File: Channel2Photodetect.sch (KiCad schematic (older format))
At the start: 5 parts

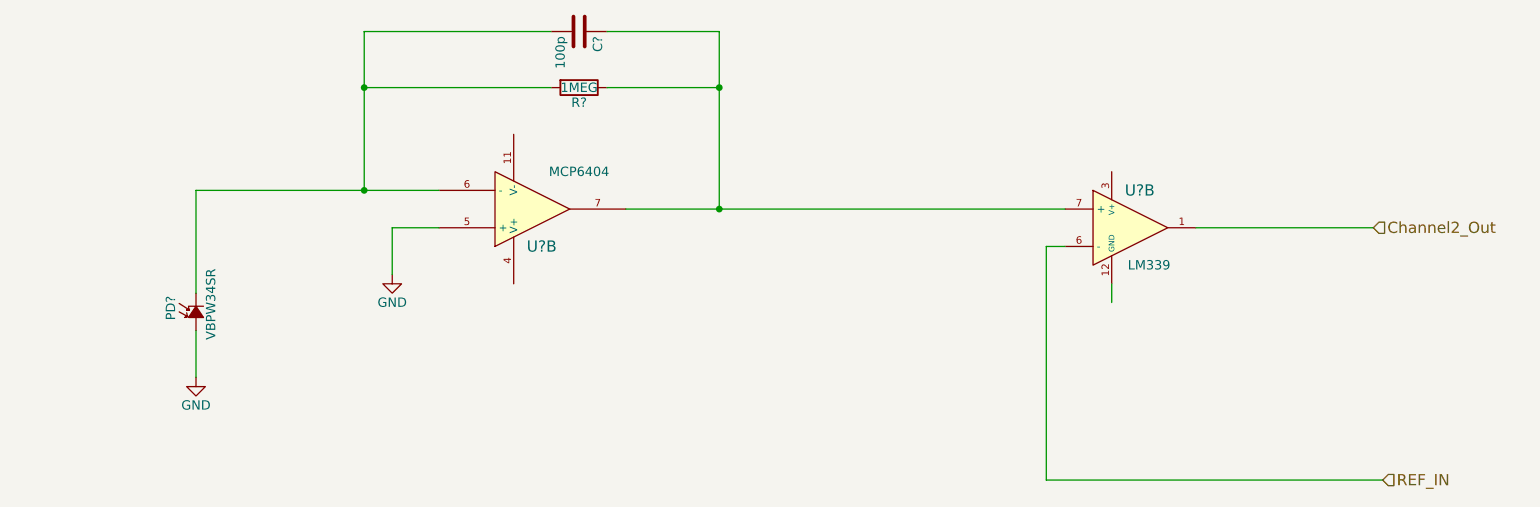
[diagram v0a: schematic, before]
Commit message: Added power regulator, VGND and test points
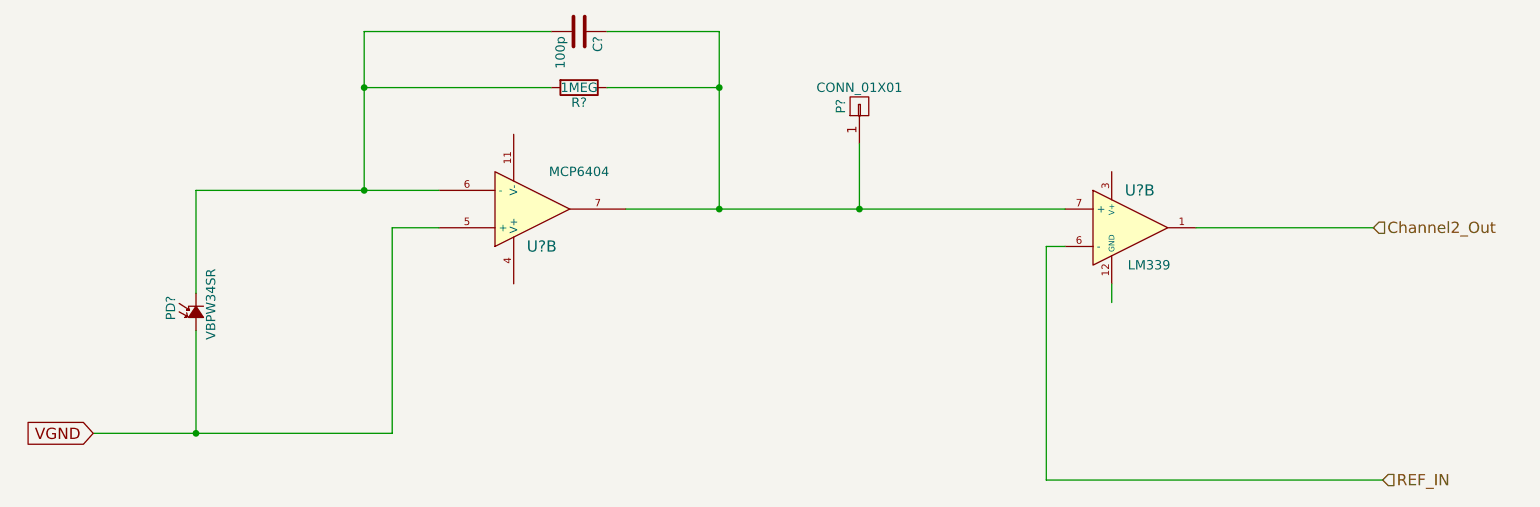
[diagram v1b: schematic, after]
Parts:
- added P?: CONN_01X01, symbol CONN_01X01
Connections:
- net labels added: VGND
- net labels removed: GND
- wire segments 17 -> 19
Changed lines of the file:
@@
 LIBS:memory
 LIBS:xilinx
-LIBS:special
 LIBS:microcontrollers
 LIBS:dsp
@@
 	4850 2200 5450 2200
 Connection ~ 5450 2500
-$Comp
-L GND #PWR?
-U 1 1 5552E303
-P 3700 3500
-F 0 "#PWR?" H 3700 3250 50  0001 C CNN
-F 1 "GND" H 3700 3350 50  0000 C CNN
-F 2 "" H 3700 3500 60  0000 C CNN
-F 3 "" H 3700 3500 60  0000 C CNN
-	1    3700 3500
-	1    0    0    -1
-$EndComp
 Wire Wire Line
 	3950 3250 3700 3250
 Wire Wire Line
-	3700 3250 3700 3500
-$Comp
-L GND #PWR?
-U 1 1 5552E31E
-P 2650 4050
-F 0 "#PWR?" H 2650 3800 50  0001 C CNN
-F 1 "GND" H 2650 3900 50  0000 C CNN
-F 2 "" H 2650 4050 60  0000 C CNN
-F 3 "" H 2650 4050 60  0000 C CNN
-	1    2650 4050
-	1    0    0    -1
-$EndComp
+	3700 3250 3700 4350
 Wire Wire Line
-	2650 3800 2650 4050
+	2650 3800 2650 4350
 $Comp
 L LM339 U?
@@
 Wire Wire Line
 	7200 4600 7200 3350
+Wire Wire Line
+	3700 4350 2100 4350
+Text GLabel 2100 4350 0    60   Input ~ 0
+VGND
+Connection ~ 2650 4350
+$Comp
+L CONN_01X01 P?
+U 1 1 55563262
+P 6200 2600
+F 0 "P?" H 6200 2700 50  0000 C CNN
+F 1 "CONN_01X01" V 6300 2600 50  0000 C CNN
+F 2 "" H 6200 2600 60  0000 C CNN
+F 3 "" H 6200 2600 60  0000 C CNN
+	1    6200 2600
+	0    -1   -1   0
+$EndComp
+Wire Wire Line
+	6200 2800 6200 3150
+Connection ~ 6200 3150
 $EndSCHEMATC

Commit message: Added libraries and imported components into the layout
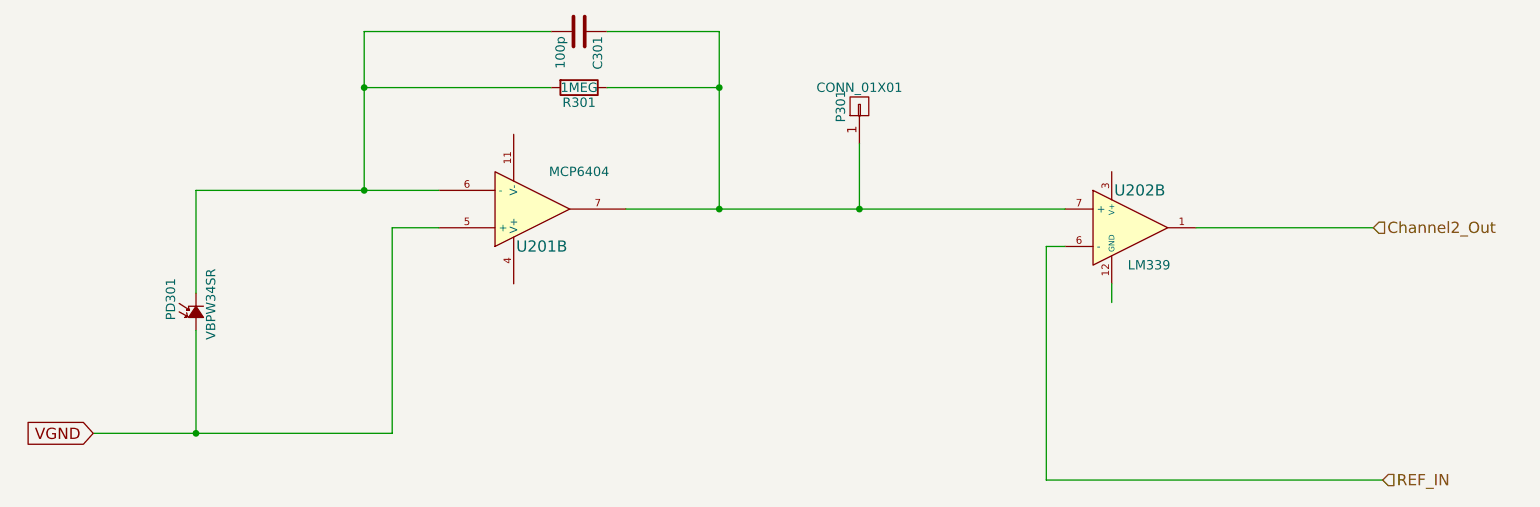
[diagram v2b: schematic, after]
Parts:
- gave numbers to parts that had none: 6
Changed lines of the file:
@@
 $EndDescr
 $Comp
-L R R?
+L R R301
 U 1 1 5552E2CE
 P 4700 2500
-F 0 "R?" V 4780 2500 50  0000 C CNN
+F 0 "R301" V 4780 2500 50  0000 C CNN
 F 1 "1MEG" V 4700 2500 50  0000 C CNN
 F 2 "" V 4630 2500 30  0000 C CNN
@@
 $EndComp
 $Comp
-L C C?
+L C C301
 U 1 1 5552E2D5
 P 4700 2200
-F 0 "C?" H 4725 2300 50  0000 L CNN
+F 0 "C301" H 4725 2300 50  0000 L CNN
 F 1 "100p" H 4725 2100 50  0000 L CNN
 F 2 "" H 4738 2050 30  0000 C CNN
@@
 $EndComp
 $Comp
-L MCP6404-E/SL U?
+L MCP6404-E/SL U201
 U 2 1 5552E2DE
 P 4450 3150
-F 0 "U?" H 4500 3350 60  0000 C CNN
+F 0 "U201" H 4500 3350 60  0000 C CNN
 F 1 "MCP6404" H 4700 2950 50  0000 C CNN
 F 2 "" H 4450 3150 60  0000 C CNN
@@
 $EndComp
 $Comp
-L Photodiode PD?
+L Photodiode PD301
 U 1 1 5552E2E7
 P 2650 3700
-F 0 "PD?" H 2605 3835 50  0000 L CNN
+F 0 "PD301" H 2605 3835 50  0000 L CNN
 F 1 "VBPW34SR" H 2500 3620 50  0000 L CNN
 F 2 "" V 2650 3700 60  0000 C CNN
@@
 	2650 3800 2650 4350
 $Comp
-L LM339 U?
+L LM339 U202
 U 2 1 5552E327
 P 7650 3250
-F 0 "U?" H 7700 3450 60  0000 C CNN
+F 0 "U202" H 7700 3450 60  0000 C CNN
 F 1 "LM339" H 7750 3050 50  0000 C CNN
 F 2 "" H 7650 3250 60  0000 C CNN
@@
 Connection ~ 2650 4350
 $Comp
-L CONN_01X01 P?
+L CONN_01X01 P301
 U 1 1 55563262
 P 6200 2600
-F 0 "P?" H 6200 2700 50  0000 C CNN
+F 0 "P301" H 6200 2700 50  0000 C CNN
 F 1 "CONN_01X01" V 6300 2600 50  0000 C CNN
 F 2 "" H 6200 2600 60  0000 C CNN

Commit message: Added photodiode component to new local footprint library
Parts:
- C301: footprint (none) -> Capacitors_SMD:C_0805_HandSoldering
- P301: footprint (none) -> Pin_Headers:Pin_Header_Straight_1x01
- PD301: footprint (none) -> DasBlinkinput:VPW34SR
- R301: footprint (none) -> Resistors_SMD:R_1206_HandSoldering
- U201, U202: footprint (none) -> Housings_SOIC:SOIC-14_3.9x8.7mm_Pitch1.27mm
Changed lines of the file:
@@
 F 0 "R301" V 4780 2500 50  0000 C CNN
 F 1 "1MEG" V 4700 2500 50  0000 C CNN
-F 2 "" V 4630 2500 30  0000 C CNN
+F 2 "Resistors_SMD:R_1206_HandSoldering" V 4630 2500 30  0001 C CNN
 F 3 "" H 4700 2500 30  0000 C CNN
 F 4 "RC1206FR-071ML" V 4700 2500 60  0001 C CNN "MPN"
@@
 F 0 "C301" H 4725 2300 50  0000 L CNN
 F 1 "100p" H 4725 2100 50  0000 L CNN
-F 2 "" H 4738 2050 30  0000 C CNN
+F 2 "Capacitors_SMD:C_0805_HandSoldering" H 4738 2050 30  0001 C CNN
 F 3 "" H 4700 2200 60  0000 C CNN
 	1    4700 2200
@@
 F 0 "U201" H 4500 3350 60  0000 C CNN
 F 1 "MCP6404" H 4700 2950 50  0000 C CNN
-F 2 "" H 4450 3150 60  0000 C CNN
+F 2 "Housings_SOIC:SOIC-14_3.9x8.7mm_Pitch1.27mm" H 4450 3150 60  0001 C CNN
 F 3 "" H 4450 3150 60  0000 C CNN
 F 4 "MCP6404-E/SL" H 4450 3150 60  0001 C CNN "MPN"
@@
 F 0 "PD301" H 2605 3835 50  0000 L CNN
 F 1 "VBPW34SR" H 2500 3620 50  0000 L CNN
-F 2 "" V 2650 3700 60  0000 C CNN
+F 2 "DasBlinkinput:VPW34SR" V 2650 3700 60  0001 C CNN
 F 3 "" V 2650 3700 60  0000 C CNN
 F 4 "VBPW34SR" H 2650 3700 60  0001 C CNN "MPN"
@@
 F 0 "U202" H 7700 3450 60  0000 C CNN
 F 1 "LM339" H 7750 3050 50  0000 C CNN
-F 2 "" H 7650 3250 60  0000 C CNN
+F 2 "Housings_SOIC:SOIC-14_3.9x8.7mm_Pitch1.27mm" H 7650 3250 60  0001 C CNN
 F 3 "" H 7650 3250 60  0000 C CNN
 F 4 "LM339DE4" H 7650 3250 60  0001 C CNN "MPN"
@@
 F 0 "P301" H 6200 2700 50  0000 C CNN
 F 1 "CONN_01X01" V 6300 2600 50  0000 C CNN
-F 2 "" H 6200 2600 60  0000 C CNN
+F 2 "Pin_Headers:Pin_Header_Straight_1x01" H 6200 2600 60  0001 C CNN
 F 3 "" H 6200 2600 60  0000 C CNN
 	1    6200 2600

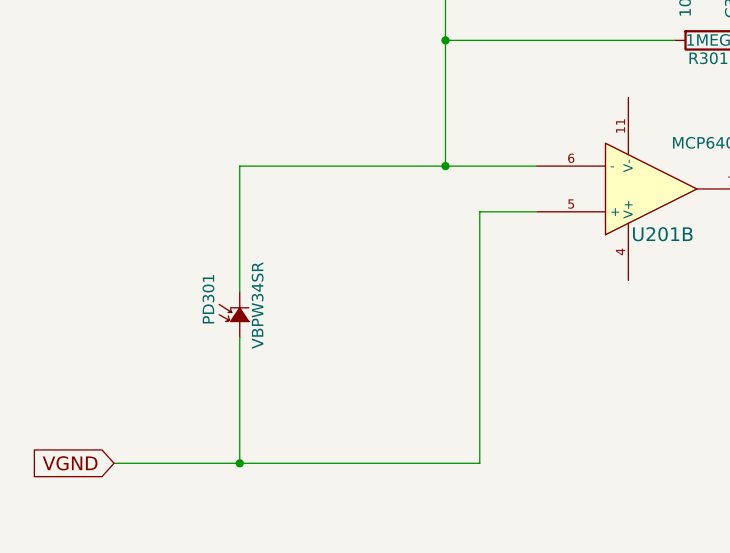
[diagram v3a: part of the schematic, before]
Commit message: Added secondary footprint for photodiode
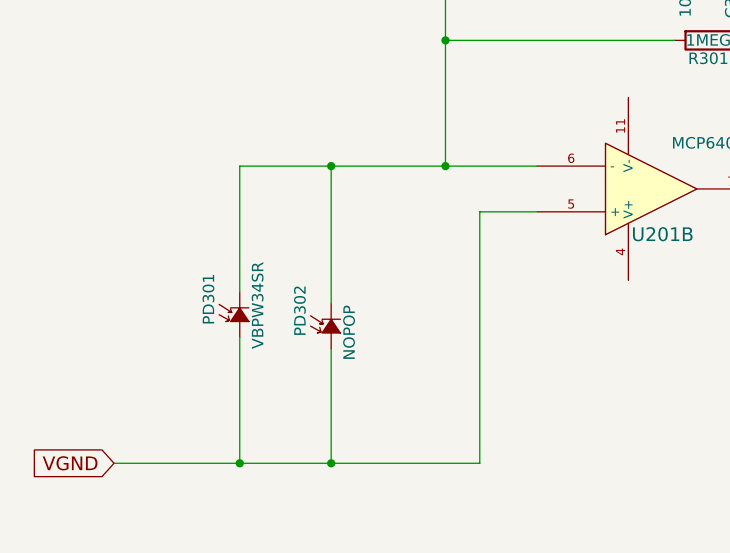
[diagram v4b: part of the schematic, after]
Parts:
- added PD302: NOPOP, Capacitors_SMD:C_0805_HandSoldering, symbol Photodiode
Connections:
- wire segments 19 -> 21
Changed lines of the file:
@@
 	6200 2800 6200 3150
 Connection ~ 6200 3150
+$Comp
+L Photodiode PD302
+U 1 1 555A3C90
+P 3050 3750
+F 0 "PD302" H 3005 3885 50  0000 L CNN
+F 1 "NOPOP" H 2900 3670 50  0000 L CNN
+F 2 "Capacitors_SMD:C_0805_HandSoldering" V 3050 3750 60  0001 C CNN
+F 3 "" V 3050 3750 60  0000 C CNN
+F 4 "TEMD6200FX01" H 3050 3750 60  0001 C CNN "MPN"
+F 5 "http://parts.io/detail/2942502/TEMD6200FX01" H 3050 3750 60  0001 C CNN "Link"
+	1    3050 3750
+	0    -1   -1   0
+$EndComp
+Wire Wire Line
+	3050 3050 3050 3650
+Wire Wire Line
+	3050 3850 3050 4350
+Connection ~ 3050 3050
+Connection ~ 3050 4350
 $EndSCHEMATC

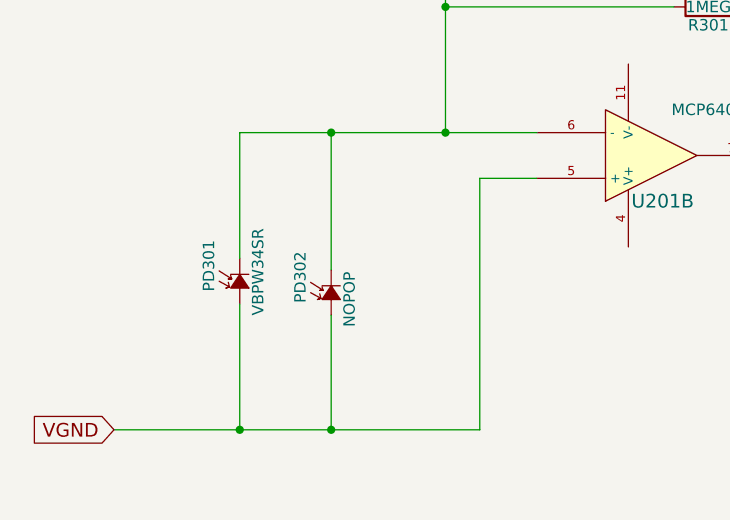
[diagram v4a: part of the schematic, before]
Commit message: Removing extra set of photodiodes and changing the original photodiode footprint
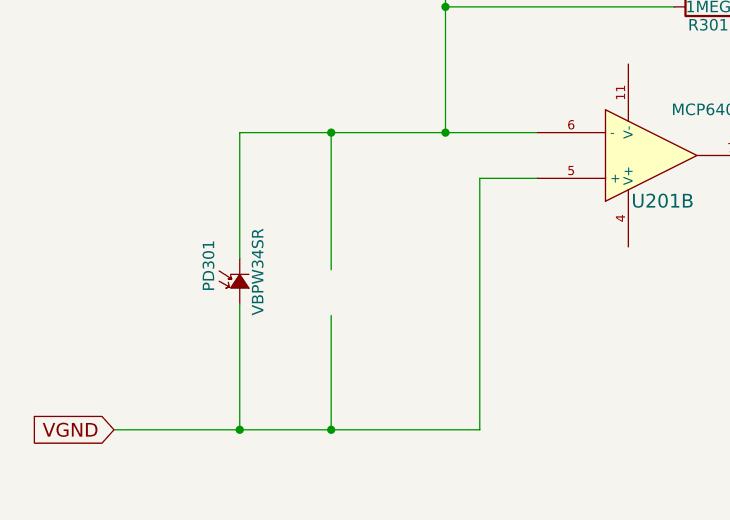
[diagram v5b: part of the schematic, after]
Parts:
- removed PD302: NOPOP, Capacitors_SMD:C_0805_HandSoldering, symbol Photodiode
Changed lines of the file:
@@
 	6200 2800 6200 3150
 Connection ~ 6200 3150
-$Comp
-L Photodiode PD302
-U 1 1 555A3C90
-P 3050 3750
-F 0 "PD302" H 3005 3885 50  0000 L CNN
-F 1 "NOPOP" H 2900 3670 50  0000 L CNN
-F 2 "Capacitors_SMD:C_0805_HandSoldering" V 3050 3750 60  0001 C CNN
-F 3 "" V 3050 3750 60  0000 C CNN
-F 4 "TEMD6200FX01" H 3050 3750 60  0001 C CNN "MPN"
-F 5 "http://parts.io/detail/2942502/TEMD6200FX01" H 3050 3750 60  0001 C CNN "Link"
-	1    3050 3750
-	0    -1   -1   0
-$EndComp
 Wire Wire Line
 	3050 3050 3050 3650

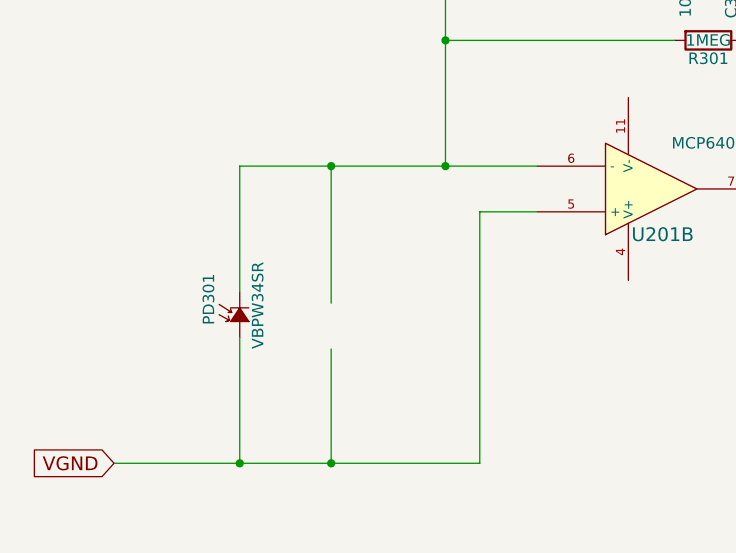
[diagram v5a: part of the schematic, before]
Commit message: Schematic and layout cleanup after photodiode removal
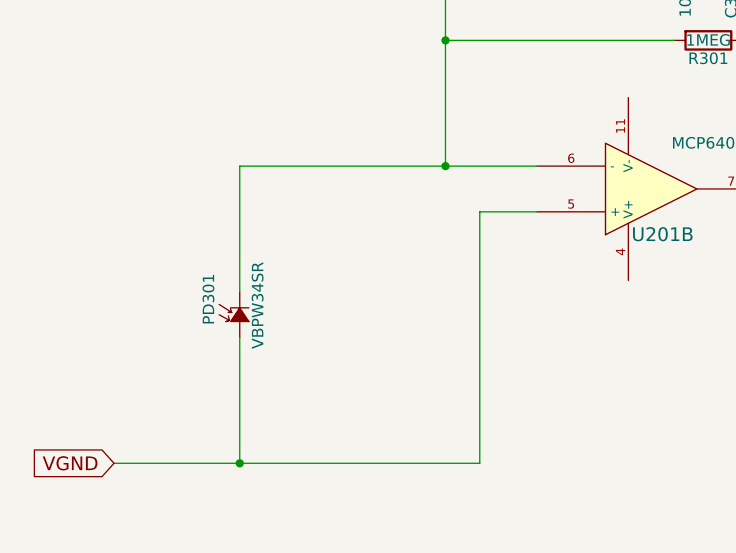
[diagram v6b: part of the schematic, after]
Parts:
- PD301: footprint DasBlinkinput:VPW34SR -> DasBlinkinput:VPW34SR*
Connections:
- wire segments 21 -> 19
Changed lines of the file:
@@
 F 0 "PD301" H 2605 3835 50  0000 L CNN
 F 1 "VBPW34SR" H 2500 3620 50  0000 L CNN
-F 2 "DasBlinkinput:VPW34SR" V 2650 3700 60  0001 C CNN
+F 2 "DasBlinkinput:VPW34SR*" V 2650 3700 60  0001 C CNN
 F 3 "" V 2650 3700 60  0000 C CNN
 F 4 "VBPW34SR" H 2650 3700 60  0001 C CNN "MPN"
@@
 	6200 2800 6200 3150
 Connection ~ 6200 3150
-Wire Wire Line
-	3050 3050 3050 3650
-Wire Wire Line
-	3050 3850 3050 4350
-Connection ~ 3050 3050
-Connection ~ 3050 4350
 $EndSCHEMATC

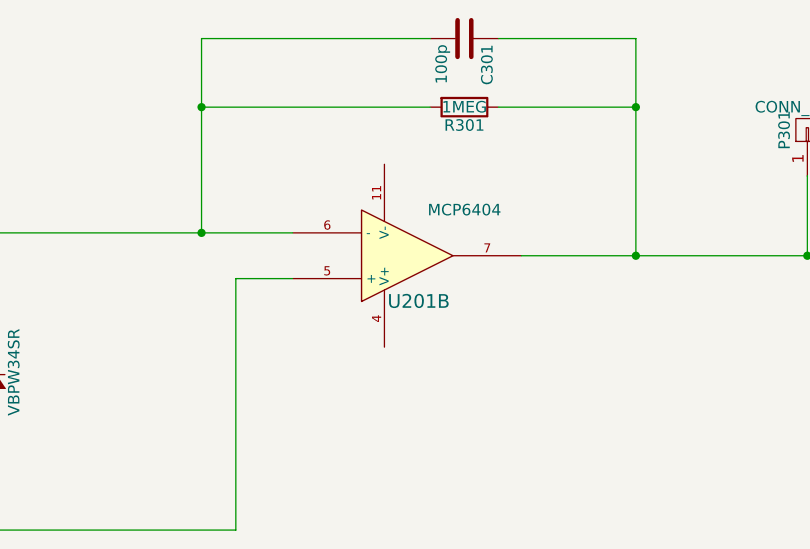
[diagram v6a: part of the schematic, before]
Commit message: Routed all passives related to U201 and the photodiodes
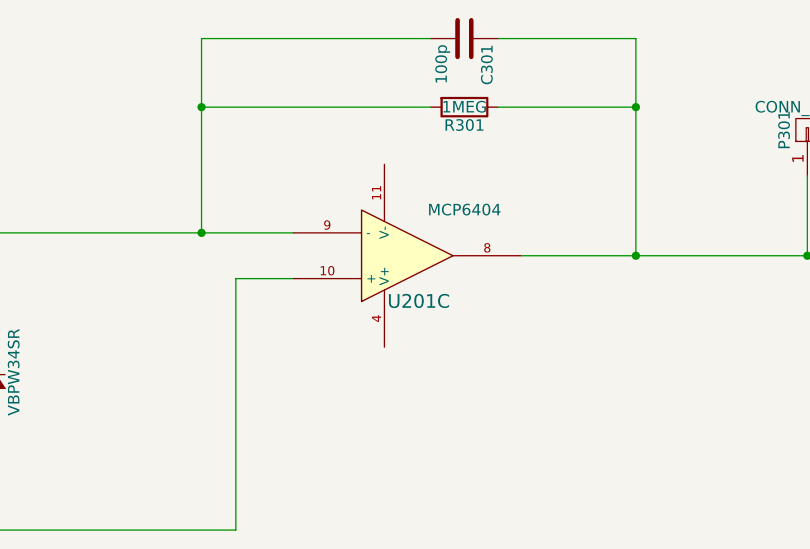
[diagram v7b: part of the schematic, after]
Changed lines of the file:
@@
 $Comp
 L MCP6404-E/SL U201
-U 2 1 5552E2DE
+U 3 1 5552E2DE
 P 4450 3150
 F 0 "U201" H 4500 3350 60  0000 C CNN
@@
 F 4 "MCP6404-E/SL" H 4450 3150 60  0001 C CNN "MPN"
 F 5 "http://parts.io/detail/3584122/MCP6404-E%2FSL" H 4450 3150 60  0001 C CNN "Link"
-	2    4450 3150
+	3    4450 3150
 	1    0    0    1
 $EndComp

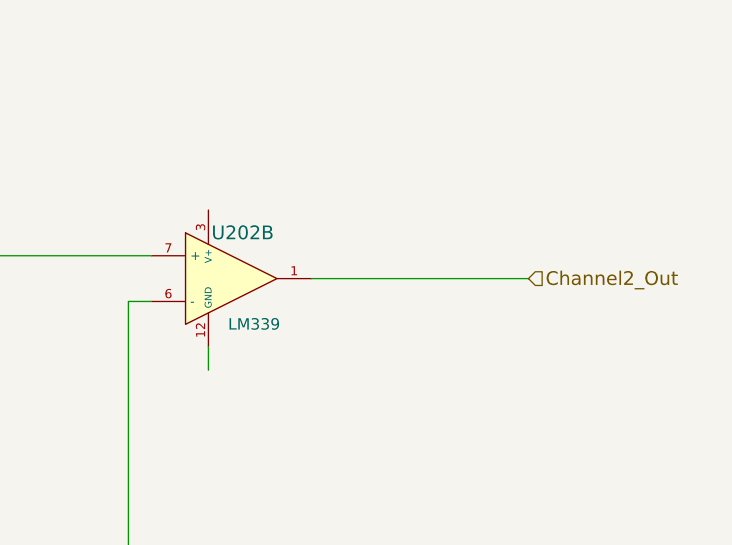
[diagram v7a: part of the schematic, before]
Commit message: Routed remainder of lines and added test points with lables
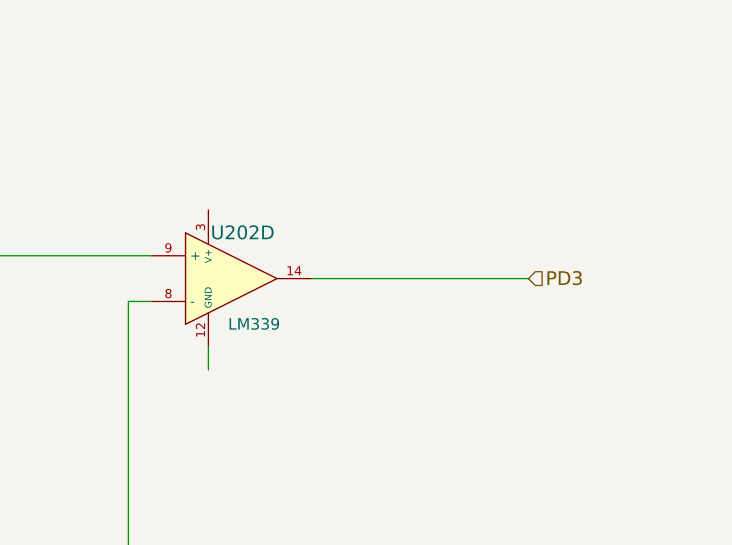
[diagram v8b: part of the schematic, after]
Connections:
- net labels added: PD3
- net labels removed: Channel2_Out
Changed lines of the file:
@@
 $Comp
 L LM339 U202
-U 2 1 5552E327
+U 4 1 5552E327
 P 7650 3250
 F 0 "U202" H 7700 3450 60  0000 C CNN
@@
 F 4 "LM339DE4" H 7650 3250 60  0001 C CNN "MPN"
 F 5 "http://parts.io/detail/916254/LM339DE4" H 7650 3250 60  0001 C CNN "Link"
-	2    7650 3250
+	4    7650 3250
 	1    0    0    -1
 $EndComp
@@
 	7550 3550 7550 3650
 Text HLabel 8950 3250 2    60   Input ~ 0
-Channel2_Out
+PD3
 Text HLabel 9000 4600 2    60   Input ~ 0
 REF_IN
